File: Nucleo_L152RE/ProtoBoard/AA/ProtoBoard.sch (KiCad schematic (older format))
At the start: 146 parts, among them J1 RJ45, J2 USB, J3 RJ45, P1 Power, P10 CONN_01X06, P11 CONN_01X04, P12 CONN_01X04, P13 CONN_02X06, P14 CONN_02X02, P15 CONN_02X02, P16 CONN_01X03, P17 CONN_01X03, P18 CONN_01X03, P19 CONN_01X04, P2 USART2, P20 CONN_01X04, P21 CONN_01X03, P22 CONN_01X03, P23 CONN_01X03, P24 CONN_01X03, P25 CONN_01X03, P26 CONN_01X03, P27 CONN_01X04, P28 Ant, P3 SWD Header, P4 USART2, P5 CONN_01X03, P6 CONN_01X04, P7 CONN_01X04, P8 CONN_01X03, P9 CONN_01X03, Q1 Q_PMOS_GSD, SW1 SW_PUSH_SMALL, U1 TPS61222-5V, U2 Nucleo-L152RE-CN7, U3 Nucleo-L152RE-CN10, U4 LM3670, U5 MT3329_GPS, U6 S25FL127S, U7 RFM69HW

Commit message: Have more of the components layout and specified.
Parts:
- removed SW1: SW_PUSH_SMALL, symbol SW_PUSH_SMALL
- added SW1: MomentarySwitch, nucleo:Tact_switch, symbol MomentarySwitch
- C10, C11, C12, C8, C9: footprint Capacitors_SMD:C_0805_HandSoldering -> (none)
- J1, J3: footprint (none) -> nucleo:RJ45_SMD
- J2: footprint (none) -> Connect:USB_B
- JP1, JP10, JP11, JP13, JP15, JP16, JP17, JP18, JP19, JP2, JP20, JP21, JP22, JP23, JP24, JP25, JP26, JP27, JP28, JP29, JP3, JP30, JP31, JP38, JP39, JP4, JP40, JP41, JP42, JP5, JP6, JP7, JP8, JP9: footprint (none) -> nucleo:SB_NC
- JP12, JP14, JP32, JP33, JP34, JP35, JP36, JP37: footprint (none) -> nucleo:SB_NO
- P1: footprint Pin_Headers:Pin_Header_Straight_1x02 -> (none)
- P28: footprint (none) -> Pin_Headers:Pin_Header_Straight_1x01
- P3: footprint Pin_Headers:Pin_Header_Straight_1x06 -> (none)
- P4: value USART2 -> USART1
- Q1: value Q_PMOS_GSD -> SI2323DS; footprint (none) -> SMD_Packages:SOT-323
- U1: footprint (none) -> nucleo:SO-70
- U4: footprint (none) -> SMD_Packages:SOT-353
- U5: footprint (none) -> nucleo:MT3329
- U6: footprint (none) -> SMD_Packages:SOIC-8-N
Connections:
- wire segments 364 -> 368

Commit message: Have all footprints selected for components, now starting to organize parts on board.
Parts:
- C1, C3, C4, C5, C6: footprint (none) -> Capacitors_SMD:C_0603_HandSoldering
- C10, C11, C12, C8, C9: footprint (none) -> Capacitors_SMD:C_0603
- C2: footprint (none) -> nucleo:Capacitor_7.2x7.2
- C7: footprint (none) -> nucleo:Cap_alum_electro_3.3x3.3
- D1, D2: footprint (none) -> nucleo:LED_0603
- J1: value RJ45 -> EXT1
- J3: value RJ45 -> EXT2
- L1: footprint (none) -> nucleo:Inductor_4.7u
- L2: footprint (none) -> nucleo:Inductor_10u
- L3, L4, R1, R10, R11, R12, R13, R14, R15, R16, R17, R18, R19, R2, R20, R21, R22, R23, R24, R25, R26, R27, R28, R29, R3, R30, R31, R32, R33, R34, R35, R36, R37, R38, R39, R4, R40, R41, R42, R43, R44, R45, R47, R5, R6, R7, R8, R9: footprint (none) -> Resistors_SMD:R_0603_HandSoldering
- P1: footprint (none) -> Pin_Headers:Pin_Header_Straight_1x02
- P10, P3: footprint (none) -> Pin_Headers:Pin_Header_Straight_1x06
- P11: value CONN_01X04 -> I2C1_B; footprint (none) -> Pin_Headers:Pin_Header_Straight_1x04
- P12: value CONN_01X04 -> I2C2_B; footprint (none) -> Pin_Headers:Pin_Header_Straight_1x04
- P13: value CONN_02X06 -> SW_1_6; footprint (none) -> Pin_Headers:Pin_Header_Straight_2x06
- P14: value CONN_02X02 -> WS_1_2; footprint (none) -> Pin_Headers:Pin_Header_Straight_2x02
- P15: value CONN_02X02 -> WS_3_4; footprint (none) -> Pin_Headers:Pin_Header_Straight_2x02
- P16: value CONN_01X03 -> MS2; footprint (none) -> Pin_Headers:Pin_Header_Straight_1x03
- P17: value CONN_01X03 -> OW1_B; footprint (none) -> Pin_Headers:Pin_Header_Straight_1x03
- P18: value CONN_01X03 -> OW2_B; footprint (none) -> Pin_Headers:Pin_Header_Straight_1x03
- P19: value CONN_01X04 -> I2C1_C; footprint (none) -> Pin_Headers:Pin_Header_Straight_1x04
- P2, P4: footprint (none) -> Pin_Headers:Pin_Header_Straight_1x04
- P20: value CONN_01X04 -> I2C2_C; footprint (none) -> Pin_Headers:Pin_Header_Straight_1x04
- P21: value CONN_01X03 -> MS3; footprint (none) -> Pin_Headers:Pin_Header_Straight_1x03
- P22: value CONN_01X03 -> OW3_A; footprint (none) -> Pin_Headers:Pin_Header_Straight_1x03
- P23: value CONN_01X03 -> OW4_A; footprint (none) -> Pin_Headers:Pin_Header_Straight_1x03
- P24: value CONN_01X03 -> MS4; footprint (none) -> Pin_Headers:Pin_Header_Straight_1x03
- P25: value CONN_01X03 -> OW3_B; footprint (none) -> Pin_Headers:Pin_Header_Straight_1x03
- P26: value CONN_01X03 -> OW4_B; footprint (none) -> Pin_Headers:Pin_Header_Straight_1x03
- P27: value CONN_01X04 -> RGB1; footprint (none) -> Pin_Headers:Pin_Header_Straight_1x04
- P5: value CONN_01X03 -> MS1; footprint (none) -> Pin_Headers:Pin_Header_Straight_1x03
- P6: value CONN_01X04 -> I2C1_A; footprint (none) -> Pin_Headers:Pin_Header_Straight_1x04
- P7: value CONN_01X04 -> I2C2_A; footprint (none) -> Pin_Headers:Pin_Header_Straight_1x04
- P8: value CONN_01X03 -> OW1_A; footprint (none) -> Pin_Headers:Pin_Header_Straight_1x03
- P9: value CONN_01X03 -> OW2_A; footprint (none) -> Pin_Headers:Pin_Header_Straight_1x03
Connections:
- net E5V renamed +5V

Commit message: Removed many jumper bridges, starting to get a feel for how many components there will be and where they will be.
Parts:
- removed J2: USB, Connect:USB_B, symbol USB
- removed JP10, JP19, JP20, JP21, JP22, JP23, JP24, JP31, JP38, JP5, JP6, JP9: Jumper_NC_Small, nucleo:SB_NC, symbol Jumper_NC_Small
- removed JP32, JP34, JP36, JP37: Jumper_NO_Small, nucleo:SB_NO, symbol Jumper_NO_Small
- removed R24, R25, R40, R41: 4.7k, Resistors_SMD:R_0603_HandSoldering, symbol R_Small
- removed R26, R27, R28, R29, R30, R31: 10k, Resistors_SMD:R_0603_HandSoldering, symbol R_Small
- added CON1: USB-MICRO-B, nucleo:USB_micro_AB, symbol USB-MICRO-B
- added D3: Green, nucleo:LED_0603, symbol Led_Small
- added D4: Blue, nucleo:LED_0603, symbol Led_Small
- added JP1: BoostEn, Pin_Headers:Pin_Header_Straight_1x02, symbol CONN_01X02
- added JP32, JP34, JP41, JP43, JP57, JP59: Jumper_NC_Small, nucleo:SB_NC, symbol Jumper_NC_Small
- added JP42, JP44, JP58, JP6, JP60, JP9: Jumper_NO_Small, nucleo:SB_NO, symbol Jumper_NO_Small
- added P2: VinPower, Pin_Headers:Pin_Header_Straight_1x02, symbol CONN_01X02
- added R10, R9: 1k, Resistors_SMD:R_0603_HandSoldering, symbol R_Small
- C2: value 100uF -> 10uF; footprint nucleo:Capacitor_7.2x7.2 -> Capacitors_SMD:C_0603_HandSoldering
- D2: value Green -> Yellow
- R17: renamed from R1; value 4.7k -> 2.2k
- R18: renamed from R2; value 4.7k -> 2.2k
- R19: renamed from R3; value 4.7k -> 2.2k
- R20: renamed from R8; value 4.7k -> 2.2k
- renumbered J3 to J2, JP11 to JP16, JP12 to JP17, JP13 to JP18, JP14 to JP19, JP1 to JP2, JP15 to JP20, JP16 to JP21, JP17 to JP22, JP18 to JP23, JP2 to JP3, JP25 to JP30, JP26 to JP31, JP27 to JP36, JP28 to JP37, JP29 to JP38, JP30 to JP39, JP3 to JP4, JP4 to JP5, JP39 to JP53, JP40 to JP54, JP41 to JP55, JP42 to JP56, L4 to L3, L3 to L4, P9 to P10, P10 to P11, P11 to P12, P12 to P13, P13 to P14, P14 to P15, P15 to P16, P16 to P17, P17 to P18, P18 to P19, P19 to P20, P20 to P21, P21 to P22, P22 to P23, P23 to P24, P24 to P25, P25 to P26, P26 to P27, P27 to P28, P28 to P29, P2 to P3, P3 to P4, P4 to P5, P5 to P6, P6 to P7, P7 to P8, P8 to P9, R4 to R1, R47 to R11, R9 to R12, R12 to R13, R13 to R14, R14 to R15, R15 to R16, R5 to R2, R16 to R21, R17 to R22, R18 to R23, R19 to R24, R20 to R25, R21 to R26, R22 to R27, R23 to R28, R6 to R3, R32 to R35, R33 to R36, R34 to R37, R35 to R38, R36 to R39, R7 to R4, R37 to R40, R38 to R41, R39 to R42, R42 to R43, R43 to R44, R10 to R5, R11 to R6, R44 to R7, R45 to R8
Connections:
- net +3V3: now also P14.10 (P10), P14.12 (P12), P14.2 (P2), P14.4 (P4), P14.6 (P6), P14.8 (P8), U2.26 (NC_[3.3v_to_other_daughterboards]), U7.8 (3.3V), JP32.1, JP34.1, JP41.2, JP43.2, JP57.2, JP59.2; no longer P10.1 (P1), P12.1 (P1), P13.1 (P1), P18.1 (P1), P19.1 (P1), P20.1 (P1), P21.1 (P1), P23.1 (P1), P24.1 (P1), P26.1 (P1), P27.1 (P1), P7.1 (P1), P8.1 (P1), P9.1 (P1), R17.1, R18.1, R19.1, R20.1, R26.2, R27.2, R40.2, R41.2
- net EXT1_ADC: now also J1.7
- net EXT1_GPIO: now also J1.8
- net EXT1_SPI_CS: now also J1.3
- net EXT2_ADC: now also J2.7
- net EXT2_GPIO: now also J2.8
- net EXT2_SPI_CS: now also J2.3
- net EXT_SPI_CLK: now also J1.4, J2.4
- net EXT_SPI_MISO: now also J1.6, J2.6; no longer JP8.1
- net EXT_SPI_MOSI: now also J1.5, J2.5; no longer JP7.1
- net GND: now also CON1.5 (GND), D3.2 (C), D4.2 (C), JP9.1, P2.2 (P2)
- net I2C_SCL1: now also R17.2; no longer R19.2
- net I2C_SDA1: now also R19.2; no longer R17.2
- net StatusLed2: now also JP8.1
- net U5V: now also JP7.1; no longer R11.2
- net USB_DM: now also R12.1; no longer R5.1
- net USB_DP: now also R5.1; no longer R12.1
- net at U7.1 (Reset): now also R39.2
- net at U7.2 (DIO0): now also P11.1 (P1)
- net at U7.3 (DIO1): now also P11.2 (P2); no longer JP33.2
- net at U7.4 (DIO2): now also P11.3 (P3)
- net at U7.5 (DIO3): now also P11.4 (P4); no longer JP35.2
- net at U7.6 (DIO4): now also P11.5 (P5)
- net at U7.7 (DIO5): now also P11.6 (P6)
- net VIN: now reaches U2.24 (VIN[6.5_TO_15v])
- net VIN: now also P2.1 (P1)
- net E5V: now reaches JP33.1
- net E5V: now also C4.1, JP35.1, U2.6 (E5V[4.3_to_5.5v]), U4.1 (VIN), JP1.1 (P1), JP42.2, JP44.2, JP58.2, JP6.1, JP60.2; no longer P11.2 (P2)
- net at R11.1: now also CON1.1 (VBUS)
- net at JP7.2: now also R11.2, JP6.2; no longer J1.5
- net at JP8.2: now also CON1.4 (ID), JP9.2; no longer J1.6
- net at R5.2: now also CON1.3 (D+)
- net at R12.2: now also CON1.2 (D-)
- net GNDPWR: now reaches L4.1
- net GNDPWR: now also L3.1, CON1.6 (SHELL1), CON1.7 (SHELL2), CON1.8 (SHELL3), CON1.9 (SHELL4)
- net +5V: no longer names the net of C3.1, U1.2 (FB), U1.4 (VOUT)
- net +5V: now also JP1.2 (P2); no longer C4.1, U2.6 (E5V[4.3_to_5.5v]), U4.1 (VIN)
- net GPS_3D renamed StatusLed4
- net StatusLed4: now also R10.1
- net GPS_Enable renamed StatusLed3
- net StatusLed3: now also R9.1
- new net: JP41.1, JP42.1, P18.1 (P1), P9.1 (P1), R26.2
- new net: JP43.1, JP44.1, P10.1 (P1), P19.1 (P1), R27.2
- new net: JP57.1, JP58.1, P23.1 (P1), P26.1 (P1), R40.2
- new net: JP59.1, JP60.1, P24.1 (P1), P27.1 (P1), R41.2
- new net: JP32.2, JP33.2, P12.1 (P1), P20.1 (P1), P7.1 (P1), R17.1, R19.1
- new net: JP34.2, JP35.2, P13.1 (P1), P21.1 (P1), P8.1 (P1), R18.1, R20.1
- new net: D3.1 (A), R9.2
- new net: D4.1 (A), R10.2
- no-connect marks 13 -> 11
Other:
- note added: "Can be powered from USB if\n U5V connected\nCan Provide power to USB if\n E5V connected"
- note added: "Future boards can be powered\nusing this pin"
- note added: "GPS MT3339"
- note added: "I2C Devices"
- note added: "If VIN supplies power,\n Boost needs to be disabled \n E5V will be provided from board"
- note added: "If using E5V, won't be able to turn off i2c devices"
- note added: "If we are using USB\nstatus 2 not as important."
- note added: "PWM"
- note added: "Select PWM pins\nTweak Res"
- note added: "Since GPS will only be populated on a few units\n Use those lines for Status indicators"
- note added: "StatusLed2 Shares pin with \nUSB ID pin"
- note added: "StatusLed3 Shares pin with \nGPS Enable"
- note added: "StatusLed4 Shares pin with \nGPS 3D fix"
- note added: "Vbat 0.7 to 5.5v"
- note added: "Vin 6.5 to 15v"
- note added: "Vin Max 5.5"
- note removed: "GPS?"
- note removed: "I2C sensors\n Ensure pullups for each i2c bus"
- note removed: "Select PWM pins"
- note removed: "USB Device with B connector similiar to printer\nNeed to be able to connect this with battery power"
- moved on the sheet: JP16, JP17, JP18, JP19, L3, L4, P1, P10, P19, P24, P27, R11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

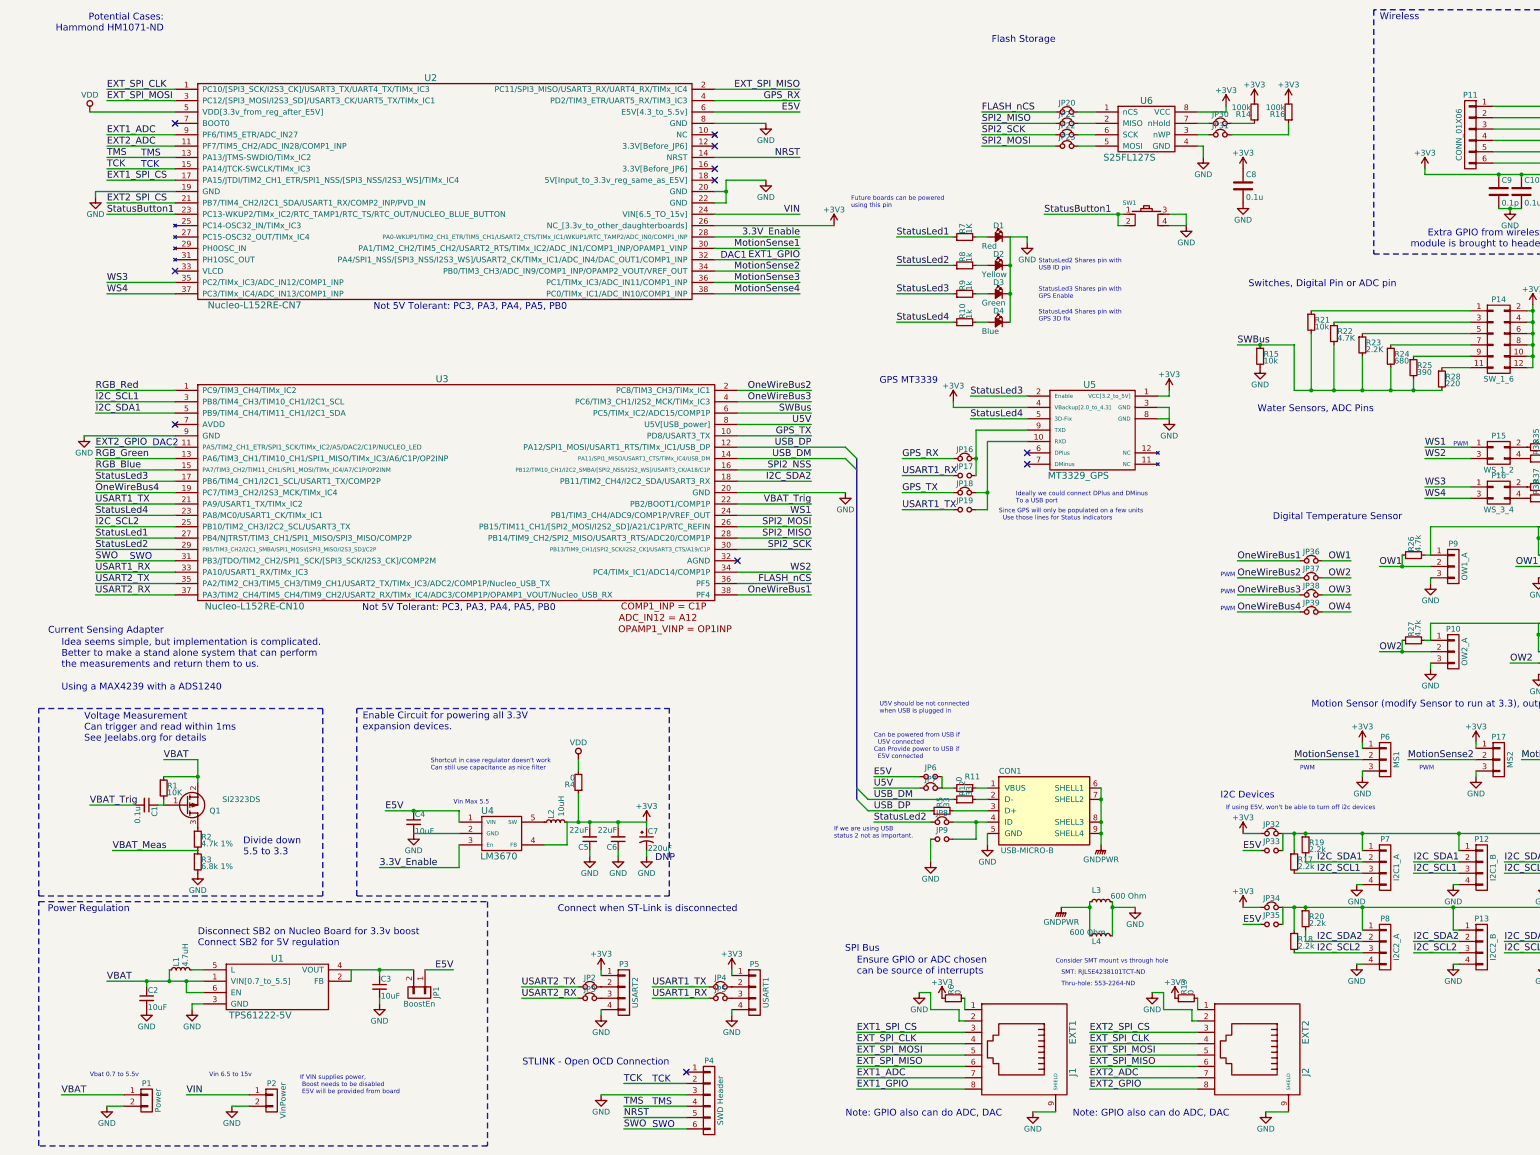
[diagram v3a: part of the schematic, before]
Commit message: About to remove a few extra connectors.
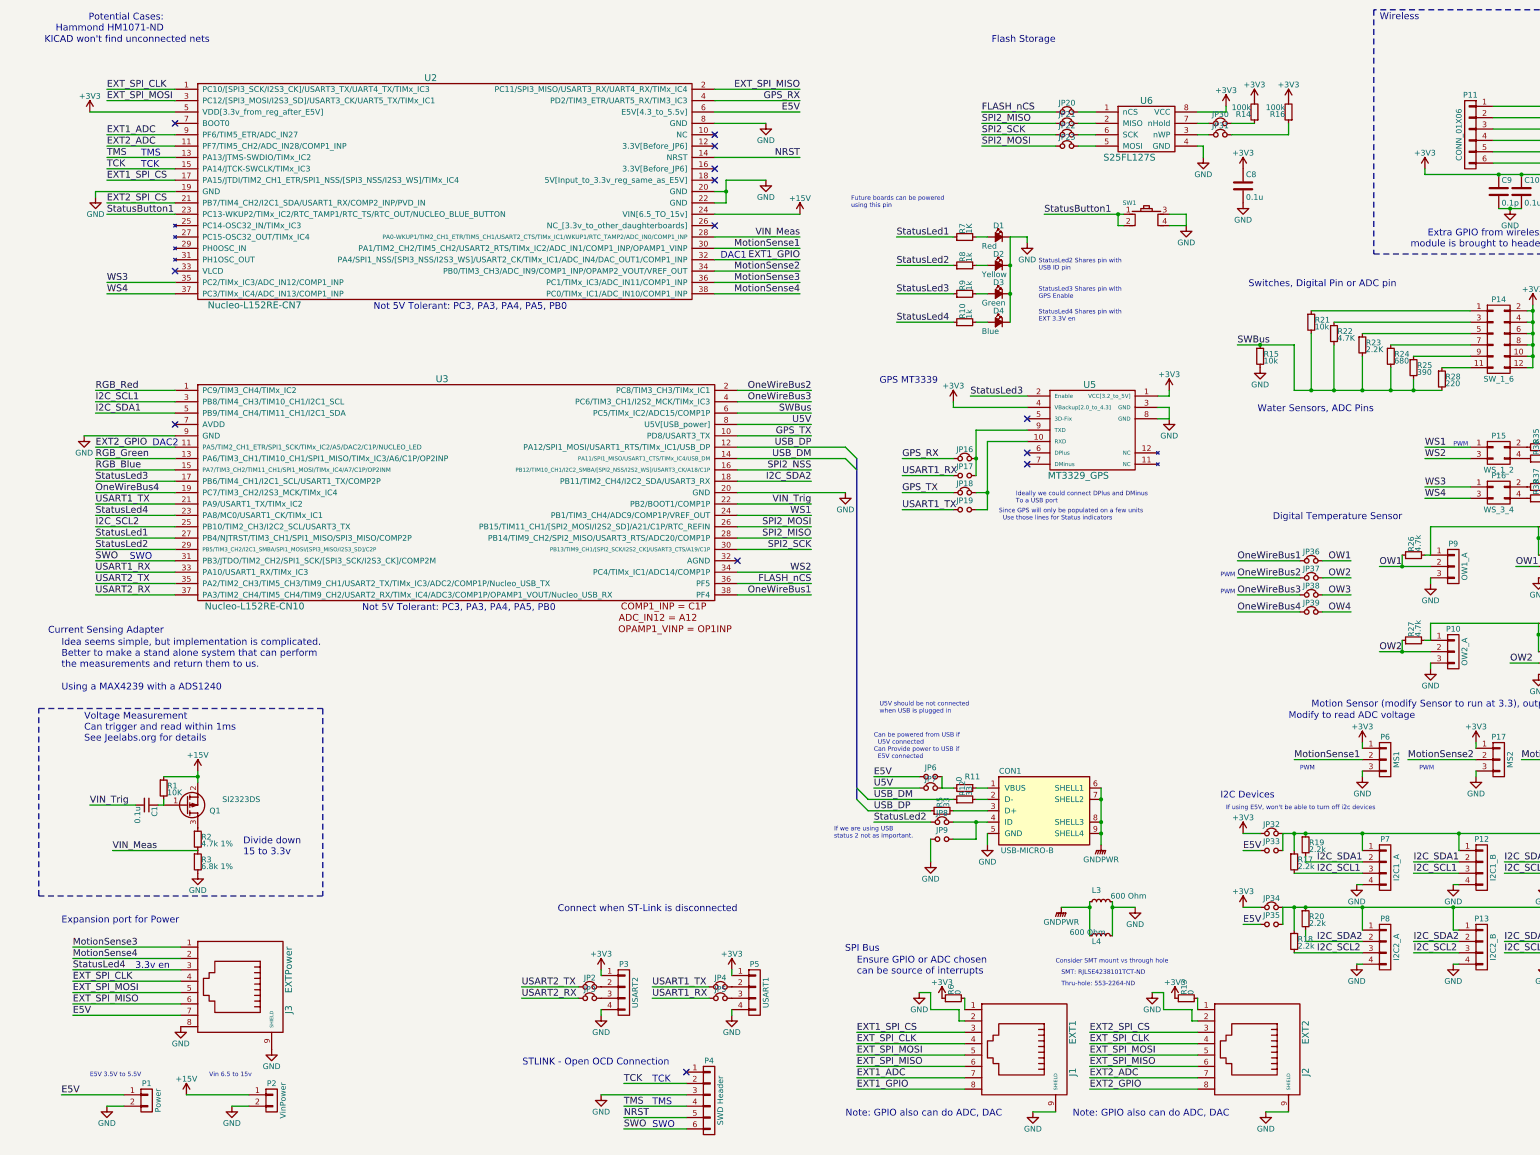
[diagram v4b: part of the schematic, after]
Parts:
- removed C2, C3, C4: 10uF, Capacitors_SMD:C_0603_HandSoldering, symbol C_Small
- removed C5, C6: 22uF, Capacitors_SMD:C_0603_HandSoldering, symbol C_Small
- removed C7: 220uF, nucleo:Cap_alum_electro_3.3x3.3, symbol CP1_Small
- removed JP1: BoostEn, Pin_Headers:Pin_Header_Straight_1x02, symbol CONN_01X02
- removed L1: 4.7uH, nucleo:Inductor_4.7u, symbol L_Small
- removed L2: 10uH, nucleo:Inductor_10u, symbol L_Small
- removed R4: 0, Resistors_SMD:R_0603_HandSoldering, symbol R_Small
- removed U1: TPS61222-5V, nucleo:SO-70, symbol TPS61222-5V
- removed U4: LM3670, SMD_Packages:SOT-353, symbol LM3670
- added J3: EXTPower, nucleo:RJ45_SMD, symbol RJ45
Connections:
- net VBAT_Meas is gone; now on net VIN_Meas: R2.2, R3.1
- net VDD is gone; now on net +3V3: U2.5 (VDD[3.3v_from_reg_after_E5V])
- net VIN is gone; now on net +15V: P2.1 (P1), U2.24 (VIN[6.5_TO_15v])
- net +3V3: no longer U2.26 (NC_[3.3v_to_other_daughterboards])
- net E5V: now also P1.1 (P1), J3.7
- net EXT_SPI_CLK: now also J3.4
- net EXT_SPI_MISO: now also J3.6
- net EXT_SPI_MOSI: now also J3.5
- net GND: now also J3.8, J3.9 (SHIELD)
- net MotionSense3: now also J3.1
- net MotionSense4: now also J3.2
- net StatusLed4: now also J3.3; no longer U5.5 (3D-Fix)
- net 3.3V_Enable renamed VIN_Meas
- net VBAT renamed +15V
- net +15V: no longer P1.1 (P1)
- net VBAT_Trig renamed VIN_Trig
- no-connect marks 11 -> 13
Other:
- note added: "3.3v en"
- note added: "Divide down\n15 to 3.3v"
- note added: "E5V 3.5V to 5.5V"
- note added: "Expansion port for Power"
- note added: "KICAD won't find unconnected nets\n"
- note added: "Modify to read ADC voltage"
- note added: "StatusLed4 Shares pin with \nEXT 3.3V en"
- note removed: "DNP"
- note removed: "Disconnect SB2 on Nucleo Board for 3.3v boost\nConnect SB2 for 5V regulation\n"
- note removed: "Divide down\n5.5 to 3.3"
- note removed: "Enable Circuit for powering all 3.3V\nexpansion devices."
- note removed: "If VIN supplies power,\n Boost needs to be disabled \n E5V will be provided from board"
- note removed: "Power Regulation"
- note removed: "Shortcut in case regulator doesn't work\nCan still use capacitance as nice filter"
- note removed: "StatusLed4 Shares pin with \nGPS 3D fix"
- note removed: "Vbat 0.7 to 5.5v"
- note removed: "Vin Max 5.5"
